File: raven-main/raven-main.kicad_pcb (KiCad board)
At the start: 2 copper layers, 7 parts, among them Q1 SQJQ100EL, U1 TPS563200, U3 ESP32-S3, U6 TPS7A4701xRGW

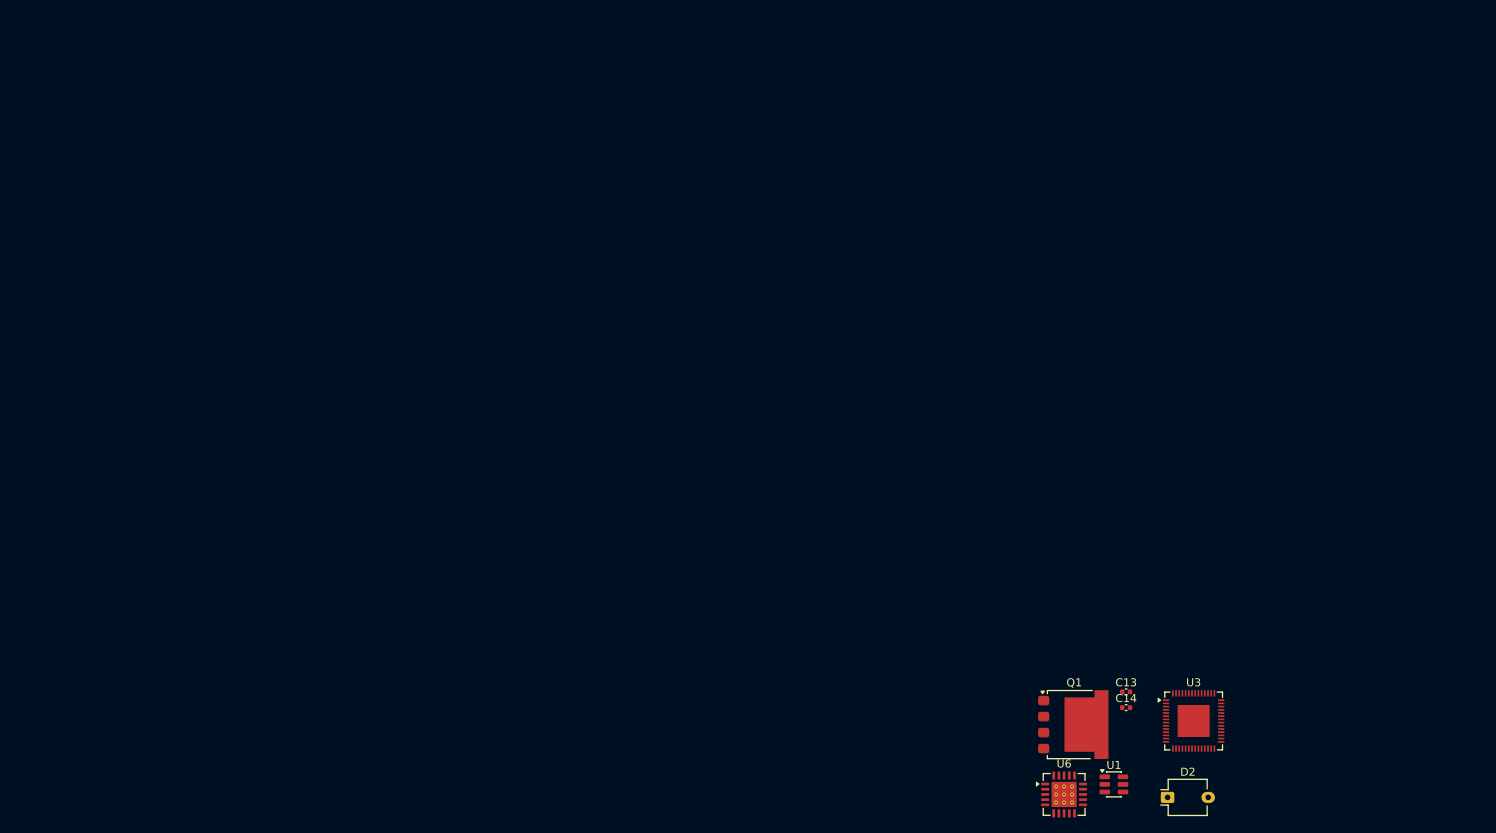
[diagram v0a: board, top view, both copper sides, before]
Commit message: Used the ESP-32 board template to create full board
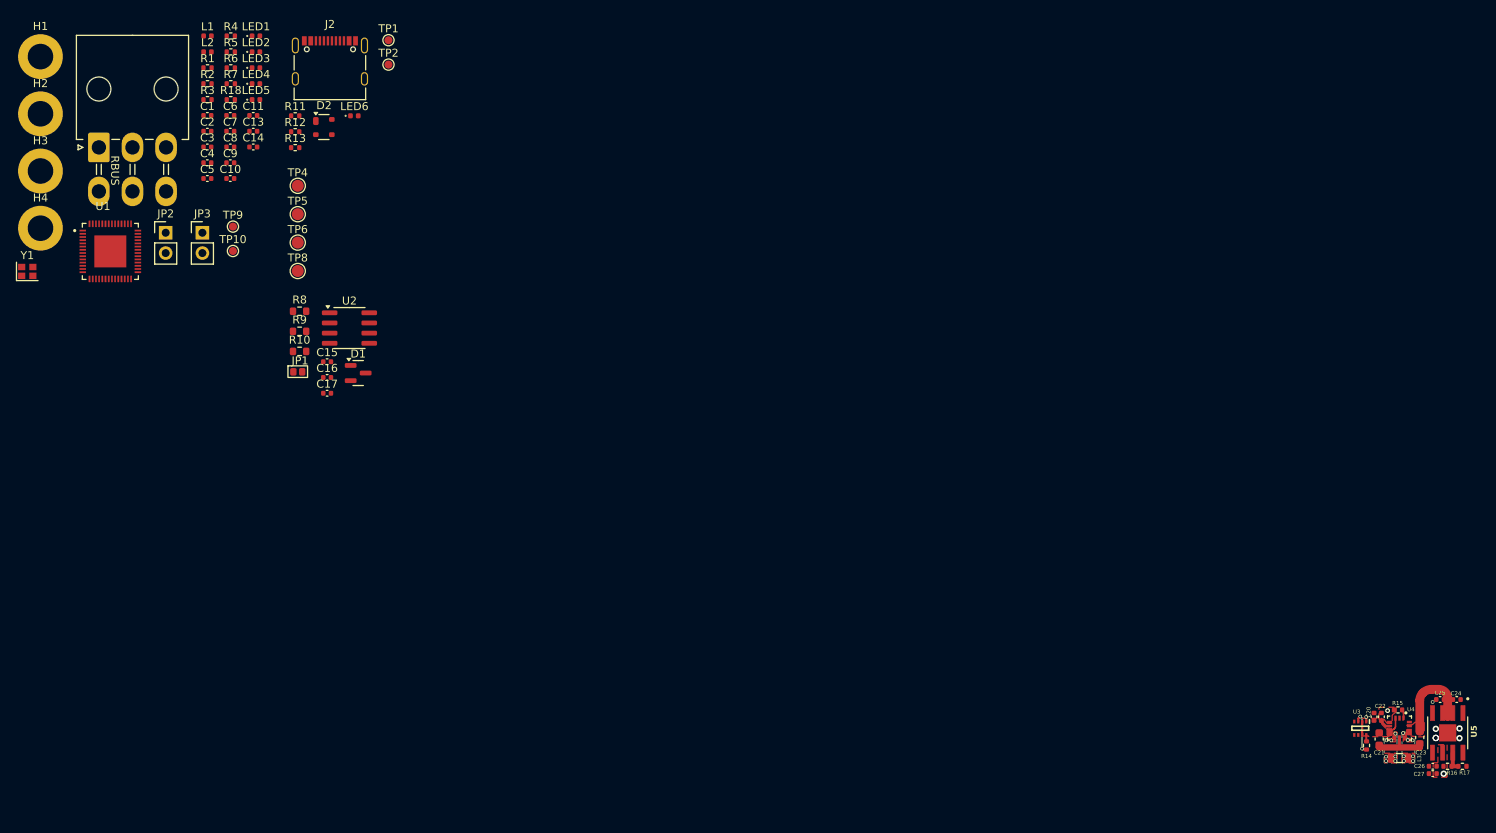
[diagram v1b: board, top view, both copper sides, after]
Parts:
- removed Q1: SQJQ100EL, Package_TO_SOT_SMD:LFPAK88
- removed U6: TPS7A4701xRGW, Package_DFN_QFN:Texas_RGW0020A_VQFN-20-1EP_5x5mm_P0.65mm_EP3.15x3.15mm_ThermalVias
- added C1: 10uF, Capacitor_SMD:C_0402_1005Metric, F.Cu at (23.9, 10.4)
- added C10: 0.1uF, Capacitor_SMD:C_0402_1005Metric, F.Cu at (26.8, 18.3)
- added C11: 0.1uF, Capacitor_SMD:C_0402_1005Metric, F.Cu at (29.7, 10.4)
- added C15: 100nF, Capacitor_SMD:C_0402_1005Metric, F.Cu at (38.9, 41.2)
- added C16: 10uF, Capacitor_SMD:C_0402_1005Metric, F.Cu at (38.9, 43.2)
- added C17: 47nF, Capacitor_SMD:C_0402_1005Metric, F.Cu at (38.9, 45.2)
- added C2: 1uF, Capacitor_SMD:C_0402_1005Metric, F.Cu at (23.9, 12.4)
- added C20: 10uF, Capacitor_SMD:C_0402_1005Metric, F.Cu at (169.8, 85.6)
- added C21: 10uF, Capacitor_SMD:C_0603_1608Metric, F.Cu at (170.4, 88.4)
- added C22: 1uF, Capacitor_SMD:C_0402_1005Metric, F.Cu at (170.7, 85.6)
- added C23: 22uF, Capacitor_SMD:C_0603_1608Metric, F.Cu at (175.5, 88.2)
- added C24: 10uF, Capacitor_SMD:C_0402_1005Metric, F.Cu at (180.1, 83.4)
- added C25: 4.7uF, Capacitor_SMD:C_0402_1005Metric, F.Cu at (178.0, 83.4)
- added C26: 10uF, Capacitor_SMD:C_0402_1005Metric, F.Cu at (177.1, 91.8)
- added C27: 0.1uF, Capacitor_SMD:C_0402_1005Metric, F.Cu at (177.1, 92.7)
- added C3: 0.1uF, Capacitor_SMD:C_0402_1005Metric, F.Cu at (23.9, 14.4)
- added C4: 1uF, Capacitor_SMD:C_0402_1005Metric, F.Cu at (23.9, 16.3)
- added C5: 0.1uF, Capacitor_SMD:C_0402_1005Metric, F.Cu at (23.9, 18.3)
- added C6: 0.1uF, Capacitor_SMD:C_0402_1005Metric, F.Cu at (26.8, 10.4)
- added C7: 1uF, Capacitor_SMD:C_0402_1005Metric, F.Cu at (26.8, 12.4)
- added C8: 0.1uF, Capacitor_SMD:C_0402_1005Metric, F.Cu at (26.8, 14.4)
- added C9: 10nF, Capacitor_SMD:C_0402_1005Metric, F.Cu at (26.8, 16.3)
- added D1: SM712_SOT23, Package_TO_SOT_SMD:SOT-23, F.Cu at (42.8, 42.6)
- added H1: MountingHole_Pad, MountingHole:MountingHole_3.2mm_M3_DIN965_Pad, F.Cu at (3.08, 3.08)
- added H2: MountingHole_Pad, MountingHole:MountingHole_3.2mm_M3_DIN965_Pad, F.Cu at (3.08, 10.2)
- added H3: MountingHole_Pad, MountingHole:MountingHole_3.2mm_M3_DIN965_Pad, F.Cu at (3.08, 17.4)
- added H4: MountingHole_Pad, MountingHole:MountingHole_3.2mm_M3_DIN965_Pad, F.Cu at (3.08, 24.5)
- added J1: RBUS, iclr:Molex_Mini-Fit_Jr_5569-06A2_2x03_P4.20mm_Horizontal, F.Cu at (10.4, 14.4)
- added J2: USB_C_Receptacle_USB2.0, iclr:USB_C_Receptacle_Palconn_UTC16-G, F.Cu at (39.3, 3.62)
- added JP1: TermJP, iclr:SmallerSolderJP, F.Cu at (35.5, 42.5)
- added JP2: Conn_01x02_Male, Connector_PinHeader_2.54mm:PinHeader_1x02_P2.54mm_Vertical, F.Cu at (18.7, 25.1)
- added JP3: Conn_01x02_Male, Connector_PinHeader_2.54mm:PinHeader_1x02_P2.54mm_Vertical, F.Cu at (23.3, 25.1)
- added L1: 2.0nH, Inductor_SMD:L_0402_1005Metric, F.Cu at (24.0, 0.49)
- added L2: 20nH, Inductor_SMD:L_0402_1005Metric, F.Cu at (24.0, 2.48)
- added L3: 1uH, Inductor_SMD:L_0805_2012Metric, F.Cu at (173.0, 90.8)
- added LED1: GREEN_LED, LED_SMD:LED_0402_1005Metric, F.Cu at (30.0, 0.49)
- added LED2: GREEN_LED, LED_SMD:LED_0402_1005Metric, F.Cu at (30.0, 2.48)
- added LED3: ORANGE_LED, LED_SMD:LED_0402_1005Metric, F.Cu at (30.0, 4.47)
- added LED4: BLUE_LED, LED_SMD:LED_0402_1005Metric, F.Cu at (30.0, 6.46)
- added LED5: RED_LED, LED_SMD:LED_0402_1005Metric, F.Cu at (30.0, 8.46)
- added LED6: WHITE_LED, LED_SMD:LED_0402_1005Metric, F.Cu at (42.3, 10.5)
- added R1: 10K, Resistor_SMD:R_0402_1005Metric, F.Cu at (24.0, 4.47)
- added R10: 60, Resistor_SMD:R_0603_1608Metric, F.Cu at (35.5, 39.9)
- added R11: 5.1k, Resistor_SMD:R_0402_1005Metric, F.Cu at (34.9, 10.5)
- added R12: 5.1k, Resistor_SMD:R_0402_1005Metric, F.Cu at (34.9, 12.5)
- added R13: 5.1k, Resistor_SMD:R_0402_1005Metric, F.Cu at (34.9, 14.5)
- added R14: 10k, Resistor_SMD:R_0402_1005Metric, F.Cu at (168.8, 89.2)
- added R15: 14k, Resistor_SMD:R_0402_1005Metric, F.Cu at (172.8, 84.7)
- added R16: 56k, Resistor_SMD:R_0402_1005Metric, F.Cu at (179.0, 91.8)
- added R17: 10k, Resistor_SMD:R_0402_1005Metric, F.Cu at (180.8, 91.8)
- added R18: 1k, Resistor_SMD:R_0402_1005Metric, F.Cu at (26.9, 8.46)
- added R2: 470, Resistor_SMD:R_0402_1005Metric, F.Cu at (24.0, 6.46)
- added R3: 10K, Resistor_SMD:R_0402_1005Metric, F.Cu at (24.0, 8.46)
- added R4: 470, Resistor_SMD:R_0402_1005Metric, F.Cu at (26.9, 0.49)
- added R5: 1k, Resistor_SMD:R_0402_1005Metric, F.Cu at (26.9, 2.48)
- added R6: 499R, Resistor_SMD:R_0402_1005Metric, F.Cu at (26.9, 4.47)
- added R7: 3k, Resistor_SMD:R_0402_1005Metric, F.Cu at (26.9, 6.46)
- added R8: 0, Resistor_SMD:R_0603_1608Metric, F.Cu at (35.5, 34.9)
- added R9: 60, Resistor_SMD:R_0603_1608Metric, F.Cu at (35.5, 37.4)
- added TP1: TestPoint, TestPoint:TestPoint_Pad_D1.0mm, F.Cu at (46.6, 1.02)
- added TP10: TestPoint, TestPoint:TestPoint_Pad_D1.0mm, F.Cu at (27.1, 27.4)
- added TP2: TestPoint, TestPoint:TestPoint_Pad_D1.0mm, F.Cu at (46.6, 4.08)
- added TP4: TestPoint, TestPoint:TestPoint_Pad_D1.5mm, F.Cu at (35.2, 19.2)
- added TP5: TestPoint, TestPoint:TestPoint_Pad_D1.5mm, F.Cu at (35.2, 22.8)
- added TP6: TestPoint, TestPoint:TestPoint_Pad_D1.5mm, F.Cu at (35.2, 26.3)
- added TP8: TestPoint, TestPoint:TestPoint_Pad_D1.5mm, F.Cu at (35.2, 29.9)
- added TP9: TestPoint, TestPoint:TestPoint_Pad_D1.0mm, F.Cu at (27.1, 24.3)
- added U2: SN65HVD230, Package_SO:SOIC-8_3.9x4.9mm_P1.27mm, F.Cu at (41.7, 37.0)
- added U4: MAX77827AEFD+T, iclr:CONV_MAX77827AEFD+T, F.Cu at (173.0, 87.0)
- added U5: SC4215ASTRT, iclr:SOIC127P599X175-9N, F.Cu at (179.0, 87.6)
- added Y1: R940000171, iclr:Crystal_SMD_2016-4Pin_2.0x1.6mm, F.Cu at (1.43, 29.9)
- C13: value 10uF -> 11pF
- C14: value 22uF -> 11pF
- D2: value BPW34 -> SP0503BAHT; footprint OptoDevice:Osram_DIL2_4.3x4.65mm_P5.08mm -> Package_TO_SOT_SMD:SOT-143
- U1: value TPS563200 -> ESP32-S3; footprint Package_TO_SOT_SMD:SOT-23-6 -> iclr:QFN40P700X700X90-57N
- U3: value ESP32-S3 -> LM66200DRLR; footprint Package_DFN_QFN:QFN-56-1EP_7x7mm_P0.4mm_EP4x4mm -> iclr:SOTFL50P160X60-8N
- moved U1 142.0 mm to (11.8, 27.4)
- moved D2 134.7 mm to (38.5, 11.9)
- moved C13 129.7 mm to (29.7, 12.4)
- moved C14 129.7 mm to (29.7, 14.4)
- moved U3 20.8 mm to (168.1, 87.0), turned to -90 degrees
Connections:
- C13 pad 1: GND -> Net-(U1-XTAL_N)
- C14 pad 1: /3.3V -> Net-(C14-Pad1)
- D2 pad 2: Net-(D2-A) -> VBUS
- U1 pad 1: GND -> unconnected-(U1-LNA_IN/RF-Pad1)
- U1 pad 2: Net-(U1-SW) -> Net-(C6-Pad1)
- U1 pad 3: GND -> Net-(C6-Pad1)
- U1 pad 4: Net-(U1-VFB) -> /CHIP_PU
- U1 pad 5: GND -> /BOOT
- U1 pad 6: Net-(U1-VBST) -> unconnected-(U1-GPIO1/ADC1_CH0-Pad6)
- U3 pad 1: unconnected-(U3-LNA_IN-Pad1) -> GND
- U3 pad 2: Net-(U3-VDD3P3-Pad2) -> /Power/BBIN
- U3 pad 3: Net-(U3-VDD3P3-Pad2) -> VBUS
- U3 pad 4: unconnected-(U3-CHIP_PU-Pad4) -> GND
- U3 pad 5: /Detector_Out -> GND
- U3 pad 6: unconnected-(U3-GPIO1-Pad6) -> RBUS_uC_V
- U3 pad 7: unconnected-(U3-GPIO2-Pad7) -> /Power/BBIN
- U3 pad 8: unconnected-(U3-GPIO3-Pad8) -> Net-(U3-ST)
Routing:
- net /Power/BBOUT: track 0.00 -> 12.3 mm
- net GND: track 0.00 -> 7.31 mm, vias 0 -> 8
- net VBUS: track 0.00 -> 5.51 mm, vias 0 -> 2
- net /Power/BBIN: track 0.00 -> 3.68 mm
- net /Power/FBIn: track 0.00 -> 2.61 mm
- net /Power/BIAS: track 0.00 -> 1.42 mm
- net /Power/SEL: track 0.00 -> 1.01 mm
- net Net-(U3-ST): track 0.00 -> 0.81 mm
- net /Power/LX2: vias 0 -> 7
- net /Power/LX1: vias 0 -> 7
- net +3V3: vias 0 -> 1
- added copper zone on F.Cu, net +3V3
- added copper zone on F.Cu, net /Power/BBIN
- added copper zone on F.Cu, net /Power/BBOUT
- added copper zone on B.Cu, net /Power/LX1
- added copper zone on F.Cu, net /Power/LX1
- added copper zone on B.Cu, net /Power/LX2
- added copper zone on F.Cu, net /Power/LX2
- added copper zone on F.Cu, net GND
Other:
- copper layers 2 -> 4
